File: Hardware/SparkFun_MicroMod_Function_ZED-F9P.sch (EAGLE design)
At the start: 121 parts, among them J2 MICROMOD_STANDARD, J3 QWIIC_RA, J4 U.FL, Q1 DMP21D0UT, U1 EEPROM, U2 U-BLOX_ZED-F9P, U3 FIN1017MXSOIC-8, U4 SN74AUP1T04DCK, U5 PCA9306DCUR, U6 74LVC541ABQ, U7 MIC5219 3.3V, U8 MIC5219 3.3V, U9 74LVC541ABQ

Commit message: Changed power resistor, needed higher power rating.
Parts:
- removed R22: 20, SparkFun-Resistors:20OHM-0603-1/10W-1%
- added R27: RK73H2ETTD16R9F, MicroMod_Function_GNSS_ublox_ZED_F9P:RK73H2ETTD16R9F
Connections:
- net ANT_!SHORT!: now also R27.1; no longer R22.1
- net N$49: now also R27.2; no longer R22.2
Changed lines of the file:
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@@
 <part name="R25" library="SparkFun-Resistors" deviceset="10KOHM" device="-0603-1/10W-1%" value="10k"/>
 <part name="L1" library="MicroMod_Function_GNSS_ublox_ZED_F9P" deviceset="LQW15AWR15J80D" device=""/>
-<part name="R22" library="SparkFun-Resistors" deviceset="20OHM" device="-0603-1/10W-1%" value="20"/>
 <part name="R23" library="SparkFun-Resistors" deviceset="2.0KOHM" device="-0603-1/10W-5%" value="2.0k"/>
 <part name="SUPPLY34" library="SparkFun-PowerSymbols" deviceset="VDD" device=""/>
@@
 <part name="TP19" library="SparkFun-Connectors" deviceset="TEST-POINT" device="3"/>
 <part name="TP20" library="SparkFun-Connectors" deviceset="TEST-POINT" device="3"/>
+<part name="R27" library="MicroMod_Function_GNSS_ublox_ZED_F9P" deviceset="RK73H2ETTD16R9F" device=""/>
 </parts>
 <sheets>
@@
 <attribute name="INDUCTANCE" x="228.6" y="223.52" size="2.032" layer="96" font="vector"/>
 </instance>
-<instance part="R22" gate="G$1" x="200.66" y="226.06" smashed="yes">
-<attribute name="NAME" x="200.66" y="227.584" size="1.778" layer="95" font="vector" align="bottom-center"/>
-<attribute name="VALUE" x="200.66" y="224.536" size="1.778" layer="96" font="vector" align="top-center"/>
-</instance>
 <instance part="R23" gate="G$1" x="190.5" y="203.2" smashed="yes" rot="R90">
 <attribute name="NAME" x="188.976" y="203.2" size="1.778" layer="95" font="vector" rot="R90" align="bottom-center"/>
@@
 <instance part="TP20" gate="G$1" x="152.4" y="236.22" smashed="yes" rot="R90">
 <attribute name="NAME" x="149.86" y="241.3" size="1.778" layer="95" font="vector"/>
+</instance>
+<instance part="R27" gate="G$1" x="200.66" y="226.06" smashed="yes">
+<attribute name="NAME" x="200.66" y="227.584" size="1.778" layer="95" font="vector" align="bottom-center"/>
+<attribute name="RESISTANCE" x="198.12" y="223.52" size="1.778" layer="96" font="vector"/>
 </instance>
 </instances>
@@
 <junction x="190.5" y="210.82"/>
 <label x="182.88" y="210.82" size="1.27" layer="95" rot="R180" xref="yes"/>
-<pinref part="R22" gate="G$1" pin="1"/>
 <pinref part="R23" gate="G$1" pin="2"/>
+<pinref part="R27" gate="G$1" pin="1"/>
 </segment>
 </net>
@@
 <junction x="220.98" y="226.06"/>
 <pinref part="L1" gate="G$1" pin="1"/>
-<pinref part="R22" gate="G$1" pin="2"/>
-</segment>
-</net>
+<pinref part="R27" gate="G$1" pin="2"/>
+</segment>
+</net>

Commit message: Ran ERC and updated.
Needed to re-place U3 parts. Needed to approve warnings/errors.
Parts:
- removed U$7: OPA344, SparkFun-IC-Amplifiers:OPA344
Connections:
- removed net GND2: JP10.2, JP2.2, JP3.2, JP4.1, JP5.1, JP6.1, JP8.2, JP9.2
- removed net N$13: C2.1, U1.VCC
- removed net N$18: J2.A0
- removed net N$31: J2.USB_VIN
- removed net N$33: J2.USBHOST_D-
- removed net N$34: J2.USBHOST_D+
- removed net N$35: J2.CTS
- removed net N$36: J2.RTS
- removed net N$37: J2.CAN-TX
- removed net N$38: J2.CAN-RX
- net 3.3V: now also C2.1, U1.VCC
- net ANT_DETECT: now also U$3G1.OUT; no longer U$7G1.OUT
- net GND: now also JP10.2, JP2.2, JP3.2, JP4.1, JP5.1, JP6.1, JP8.2, JP9.2
- net N$48: now also U$3G1.+IN; no longer U$7G1.+IN
- net N$49: now also U$3G1.-IN; no longer U$7G1.-IN
- net PWR_EN: now also U7.EN
- net VCC: no longer U7.EN

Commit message: Updated Schematic for ERC and comments from Paul.
Created NO jumper on USB-C shield/gnd tie.
Updated some power connections for style.
Deleted $ from designations.
Reworded ANT_OFF comment.
Repositioned ANT_!SHORT! net.
Floated U9Y7 output.
Renamed version back to v01 per SFE standards.
Changed proportional text to vector.
Ran and mitigated ERC.
Reworded LED comment.
Deleted unused wires.
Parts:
- added JP13: JUMPER-SMT_2_NO_SILK, SparkFun-Jumpers:JUMPER-SMT_2_NO_SILK
- added R22: 10k, SparkFun-Resistors:10KOHM-0603-1/10W-1%
- renumbered U$3 to U10
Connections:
- removed net N$49: C13.1, L1.1, R27.2, U10G1.-IN
- new net N$18: J1.SHLD, JP13.2
- net ANT_!SHORT!: now also C13.1, L1.1, R27.2, U10G1.-IN
- net GND: now also JP13.1; no longer J1.SHLD, U9.Y7
- net PWR_EN: now also R22.1
- net VCC: now also R22.2
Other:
- note added: "Cut jumpers to disable LEDs."
- note added: "Move R25 to R26 to use antenna supervisor."
- note added: "v01"
- note removed: "Cut jumpers to remove respective LEDs"
- note removed: "Pull ANT_OFF High to use antenna supervisor."
- note removed: "v1.0"

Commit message: Update Post schematic review.
Made all easy changes, in midst of redoing decoupling per requests.
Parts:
- removed BYP, JP7, USB_EN: JUMPER-SMT_2_NO_SILK, SparkFun-Jumpers:JUMPER-SMT_2_NO_SILK
- removed C3, C5: 470pF, SparkFun-Capacitors:470PF-0603-50V-5%
- removed C4, C6: 2.2uF, SparkFun-Capacitors:2.2UF-0603-10V-20%
- removed D1, D12, D2, D8: RED, SparkFun-LED:LED-RED0603
- removed D10: 3A/10V/280mV, SparkFun-DiscreteSemi:DIODE-SCHOTTKY-BAT60A
- removed F1: 6V/2A, SparkFun-Fuses:PPTC_6V2A
- removed JP10, JP2, JP3, JP8: JUMPER-SMT_2_NC_TRACE_SILK, SparkFun-Jumpers:JUMPER-SMT_2_NC_TRACE_SILK
- removed JP11, JP12: JUMPER-SMT_3_2-NC_TRACE_SILK, SparkFun-Jumpers:JUMPER-SMT_3_2-NC_TRACE_SILK
- removed R13, R14, R15, R16: 1.5k, SparkFun-Resistors:1.5KOHM-0603-1/10W-1%
- removed R17: 100k, SparkFun-Resistors:100KOHM-0603-1/10W-1%
- removed R19, R21, R4: 1k, SparkFun-Resistors:1KOHM-0603-1/10W-1%
- removed R22: 10k, SparkFun-Resistors:10KOHM-0603-1/10W-1%
- removed U7, U8: MIC5219 3.3V, SparkFun-IC-Power:V_REG_MIC52193.3V
- added C18: 2.2uF, SparkFun-Capacitors:2.2UF-0402_TIGHT-10V-10%-X5R
- added C19, C20: 0.1uF, SparkFun-Capacitors:0.1UF-0603-25V-(+80/-20%)
- added J8: Bus Selection, SparkFun-Connectors:CONN_03LOCK
- added J9: (no value), SparkFun-Connectors:CONN_02
- added U$21, U$22: 74LVC4066D_QUAD_BILATERAL_SWITCH, SparkFun-IC-Logic:74LVC4066D_QUAD_BILATERAL_SWITCH
- C11: device SparkFun-Capacitors:0.1UF-0402-16V-10% -> SparkFun-Capacitors:0.1UF-0603-25V-(+80/-20%)
- J4: device SparkFun-RF:ANTENNA-SMA-GROUNDEDEDGE_SMA -> SparkFun-Connectors:U.FL2PIN
- J5: value (none) -> 455-1750-1-ND; device SparkFun-Connectors:CONN_02-JST-2MM-SMT -> SparkFun-Connectors:CONN_03
- J6: device SparkFun-Connectors:CONN_01 -> SparkFun-Connectors:CONN_04PTH
- R10, R9: value 27OHM -> 27
- R27: value RK73H2ETTD16R9F -> 10; device MicroMod_Function_GNSS_ublox_ZED_F9P:RK73H2ETTD16R9F -> SparkFun-Resistors:10OHM-0603-1/10W-1%
- R3: value 1k -> 10k; device SparkFun-Resistors:1KOHM-0603-1/10W-1% -> SparkFun-Resistors:10KOHM-0603-1/10W-1%
- U9: value 74LVC541ABQ -> SN74AUP1T04DCK; device MicroMod_Function_GNSS_ublox_ZED_F9P:74LVC541ABQ -> MicroMod_Function_GNSS_ublox_ZED_F9P:SN74AUP1T04DCK
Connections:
- removed net N$11: D1.C, R3.2
- removed net N$14: C5.1, U8.BP
- removed net N$15: JP8.1, R19.1
- removed net N$16: D8.C, R19.2
- removed net N$17: C3.1, U7.BP
- removed net N$19: D10.A, USB_EN.2
- removed net N$20: BYP.1, D10.C, D9.C, F1.1
- removed net N$24: JP7.2, R17.1, U6.A7
- removed net N$39: JP10.1, R21.1
- removed net N$40: D12.C, R21.2
- removed net N$42: JP12.1, R14.2
- removed net N$43: JP11.1, R15.2
- removed net N$44: JP11.3, R16.2
- removed net N$47: JP12.3, R13.2
- removed net N$50: J5.2, U3.DO+
- removed net N$7 (its old number): D2.C, R4.2
- new net !ZED_DSEL!: U$22.1E, U$22.2E, U$22.3E, U$22.4E, U9.Y
- new net N$13: Q1.D, R23.2, R27.1
- new net PICO: U$22.4Z
- new net POCI: U$22.3Z
- new net RXI: U$21.4Z
- new net SCK: U$22.2Z
- new net SCL: U$21.2Z
- new net SDA: U$21.1Z
- new net SPI_!CS!: U$22.1Z
- new net TXO: U$21.3Z
- net !SAFEBOOT!: now also J7.1; no longer J2.F5, U6.A3
- net 3.3V: no longer D2.A, JP11.2
- net ANT_!SHORT!: no longer Q1.D, R23.2, R27.1, U6.A6
- net ANT_DETECT: no longer U6.A5
- net ANT_OFF: no longer U9.Y0
- net EXTINT: now also J9.1, U6.A3; no longer U6.A4
- net GEO_STAT: now also U6.Y6; no longer U9.Y1
- net GND: now also C11.1, C19.2, C20.2, J5.3, J6.1, J6.4, J8.3, J9.2, U$21.GND, U$22.GND; no longer C11.2, C3.2, C5.2, JP10.2, JP2.2, JP3.2, JP7.1, JP8.2, U7.GND, U8.GND, U9.A7
- net GND_RF: now also C18.2; no longer C4.2, C6.2
- net IO_!OE!: no longer U9.!OE1!, U9.!OE2!
- net N$10: now also J8.1; no longer JP2.1
- net N$51: now also J6.3; no longer J5.1
- net N$9: now also J6.2, U3.DO+; no longer JP3.1, R4.1
- net PPS: now also U6.Y5; no longer U9.Y6
- net PWR_EN: no longer R22.1, U7.EN
- net RTK_STAT: now also U6.Y7; no longer U9.Y2
- net RX/COPI: no longer U6.A1
- net RX2/RTCM: now also J5.1; no longer J2.F7, J6.1
- net SCL/SCK: no longer R16.1
- net SDA/!CS!: no longer R15.1
- net TX/CIPO: no longer U9.Y4
- net TX2/RTCM: now also J5.2, U6.Y1; no longer J2.F6, J7.1, U9.Y3
- net TX_READY: now also U6.Y4; no longer U9.Y5
- net VCC: now also D9.C; no longer BYP.2, F1.2, R22.2, U7.IN
- net VDD: now also C11.2, C19.1, C20.1, R3.2, U$21.VCC, U$22.VCC; no longer C11.1, C4.1, JP12.2, R17.2, U7.OUT, U8.EN
- net VIN: no longer D1.A
- net V_BATT: now also C18.1
- net V_USB: no longer D8.A, U8.IN, USB_EN.1
- net V_USB_2: no longer C6.1, D12.A, U8.OUT
- net ZED_!SAFEBOOT!: no longer U6.Y3
- net ZED_ANT_!SHORT!: no longer U6.Y6
- net ZED_ANT_DETECT: no longer U6.Y5
- net ZED_ANT_OFF: no longer U9.A0
- net ZED_DSEL: now also J8.2, U$21.1E, U$21.2E, U$21.3E, U$21.4E, U9.A; no longer U6.Y7
- net ZED_EXTINT: now also U6.Y3; no longer U6.Y4
- net ZED_GEO_STAT: now also U6.A6; no longer U9.A1
- net ZED_PPS: now also U6.A5; no longer U9.A6
- net ZED_RTK_STAT: now also U6.A7; no longer U9.A2
- net ZED_RX/COPI: no longer U6.Y1
- net ZED_SCL/SCK: no longer R14.1
- net ZED_SDA/!CS!: no longer R13.1
- net ZED_TX/CIPO: no longer U9.A4
- net ZED_TX2/RTCM: now also U6.A1; no longer U9.A3
- net ZED_TX_READY: now also U6.A4; no longer U9.A5
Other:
- note added: "Bus Selection: 74LVC4066D"
- note added: "Differential PPS"
- note added: "GNSS Module ZED-F9P"
- note added: "RF/Antenna Supervision"
- note added: "SPI or I2C+Serial Selection"
- note added: "The default is I2C and Serial."
- note added: "To use SPI simply move the 2-pin jumper to the side labeled "SPI"."
- note removed: "Close to enable SPI."
- note removed: "Close to enable USB power-up."
- note removed: "GPS Module ZED-F9P"
- note removed: "NO"
- note removed: "RF/ANTENNA SUPERVISION"
- note removed: "Tantalum"
- moved on the sheet: C1, C10, C11, C12, C13, C14, C15, C16, C17, C2, C7, C8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

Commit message: Complete schematic after DR changes.
Reorganized power: changed supply, removed fuse, replaced usb_det supply with voltage divider, renamed power nets.
Added TPs and PTH breakouts for some pins.
Changed I/O decoupling: Replaced octal buffer with 2x quad SSR switches, removed buffer on antenna supervision, rearranged pins on remaining octal buffer.
Labeled diff PPS signal.
Added second Qwiic connector.
Added selector headers for bus and antenna supervisor circuits.
Removed extra LEDs.
Replaced SMA with u.FL.
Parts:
- removed C16: 0.1uF, SparkFun-Capacitors:0.1UF-0603-25V-(+80/-20%)
- removed D5: BLUE, SparkFun-LED:LED-BLUE0603
- removed JP6: JUMPER-SMT_2_NC_TRACE_SILK, SparkFun-Jumpers:JUMPER-SMT_2_NC_TRACE_SILK
- removed R25: 10k, SparkFun-Resistors:10KOHM-0603-1/10W-1%
- removed R26: DNP, SparkFun-Resistors:DNP-0603_NO_CREAM
- removed TP11: TEST-POINT3, SparkFun-Connectors:TEST-POINT3
- removed U$21, U$22: 74LVC4066D_QUAD_BILATERAL_SWITCH, SparkFun-IC-Logic:74LVC4066D_QUAD_BILATERAL_SWITCH
- added C3: 1.0uF, SparkFun-Capacitors:1.0UF-0603-16V-10%
- added D1: 3A/10V/280mV, SparkFun-DiscreteSemi:DIODE-SCHOTTKY-BAT60A
- added J10: QWIIC_RA, SparkFun-Connectors:QWIIC_CONNECTORJS-1MM
- added J11: Bus Selection, SparkFun-Connectors:CONN_03LOCK
- added J12: USB Female Type C Connector, SparkFun-Connectors:USB_C_4-LAYER-ISOLATED
- added J13, J14, J15, J16, J17: (no value), SparkFun-Connectors:CONN_01
- added J18: (no value), SparkFun-Connectors:CONN_02
- added JP2: JUMPER-SMT_2_NO_SILK, SparkFun-Jumpers:JUMPER-SMT_2_NO_SILK
- added R4: 10k, SparkFun-Resistors:10KOHM-0603-1/10W-1%
- added U11, U12: 74LVC4066D_QUAD_BILATERAL_SWITCH, SparkFun-IC-Logic:74LVC4066D_QUAD_BILATERAL_SWITCH
- added U7: 3.3V, SparkFun-IC-Power:V_REG_AP2112K-3.3V
- C1: value 10pF -> 1.0uF; device SparkFun-Capacitors:10PF-0603-50V-5% -> SparkFun-Capacitors:1.0UF-0603-16V-10%
- J1: device SparkFun-Connectors:USB_C_2-LAYER_PADS -> SparkFun-Connectors:CONN_01
- R12: value 220k -> 68.1k; device SparkFun-Resistors:220KOHM-0603-1/10W-1% -> SparkFun-Resistors:68.1KOHM-0603-1/10W-1%
- R7: value 1k -> 10k; device SparkFun-Resistors:1KOHM-0603-1/10W-1% -> SparkFun-Resistors:10KOHM-0603-1/10W-1%
- TP7, TP9: value TEST-POINTPOGO_PTH -> TEST-POINT3; device SparkFun-Connectors:TEST-POINTPOGO_PTH -> SparkFun-Connectors:TEST-POINT3
- U5: value PCA9306DCUR -> SN74LVC1G66DRYR; device MicroMod_Function_GNSS_ublox_ZED_F9P:PCA9306DCUR -> MicroMod_Function_GNSS_ublox_ZED_F9P:SN74LVC1G66DRYR
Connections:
- removed net N$18: J1.SHLD, JP13.2
- removed net N$45: JP6.2, R7.1
- removed net N$46: D5.C, R7.2
- removed net PICO: U$22.4Z
- removed net POCI: U$22.3Z
- removed net RX/COPI: J2.RX, J2.SPI_SDI, TP15.1
- removed net RXI: U$21.4Z
- removed net SCK: U$22.2Z
- removed net SCL: U$21.2Z
- removed net SCL/SCK: J2.I2C_SCL, J2.SPI_SCK, J3.4, TP19.1, U1.SCL, U5.SCL1
- removed net SDA: U$21.1Z
- removed net SDA/!CS!: J2.F1/!CS!, J2.I2C_SDA, J3.3, TP20.1, U1.SDA, U5.SDA1
- removed net SPI_!CS!: U$22.1Z
- removed net TX/CIPO: J2.SPI_SDO, J2.TX, TP16.1
- removed net TXO: U$21.3Z
- removed net VCC: C12.1, D9.C, TP6.1, U3.VCC
- removed net V_USB_2: C7.1, C8.1, R18.2, TP11.1, U2.V_USB
- new net 5V: C3.1, D1.C, D9.C, U5.CTRL_IN, U5.VCC, U7.IN
- new net MM_!CS!: J2.F1/!CS!, TP8.1, U12.1Z
- new net MM_CIPO: J2.SPI_SDO, TP6.1, U12.3Z
- new net MM_COPI: J2.SPI_SDI, TP2.1, U12.4Z
- new net MM_RX: J2.RX, TP15.1, U11.4Z
- new net MM_SCK: J2.SPI_SCK, TP7.1, U12.2Z
- new net MM_SCL: J10.4, J2.I2C_SCL, J3.4, TP19.1, U1.SCL, U11.2Z
- new net MM_SDA: J10.3, J2.I2C_SDA, J3.3, TP20.1, U1.SDA, U11.1Z
- new net MM_TX: J2.TX, TP16.1, U11.3Z
- new net N$11: J11.1, R4.1
- new net N$16: D1.A, JP2.2
- new net SHLD: J12.SHLD, JP13.1
- new net V_ZED: C10.1, C11.2, C14.2, C17.2, C19.1, C20.1, C9.1, D11.A, U10G2.P$V+, U11.VCC, U12.VCC, U2.VCC, U4.A, U4.VCC, U6.VCC, U9.VCC
- new net ZED_USB_DET: C7.1, C8.1, R12.1, R12.2, R18.2, U2.V_USB, U5.A_OUT
- net !RESET!: now also J18.1, U6.A1; no longer U6.A2
- net !ZED_DSEL!: now also U12.1E, U12.2E, U12.3E, U12.4E; no longer U$22.1E, U$22.2E, U$22.3E, U$22.4E
- net 3.3V: now also C12.1, J10.2, U3.VCC; no longer C16.1, TP8.1, U5.VREF1
- net ANT_OFF: now also J11.2; no longer R25.2, R26.1
- net EXTINT: now also TP10.1, U6.A2; no longer U6.A3
- net GEO_STAT: now also J2.F5, U6.Y7; no longer D5.A, U6.Y6
- net GND: now also C3.2, J10.1, J12.GND, J13.1, J14.1, J18.2, JP13.2, U5.VSS, U7.GND; no longer C10.2, C11.1, C16.2, C17.1, C19.2, C20.2, J1.GND, J8.3, JP13.1, JP6.1, TP2.1, TP7.1, U$21.GND, U$22.GND, U4.GND, U5.GND, U6.GND, U9.GND
- net GND_RF: now also C10.2, C11.1, C17.1, C19.2, C20.2, J15.1, J16.1, J8.3, R7.1, U11.GND, U12.GND, U4.GND, U6.GND, U9.GND; no longer R25.1, TP9.1
- net N$1: now also J12.D+; no longer J1.D+
- net N$12: now also J11.3, R7.2; no longer C1.1, R12.1, U5.EN, U5.VREF2
- net N$2: now also J12.D-; no longer J1.D-
- net N$3: now also J12.CC2; no longer J1.CC2
- net N$4: now also J12.CC1; no longer J1.CC1
- net PPS: now also U6.Y0; no longer U6.Y5
- net PWR_EN: now also U7.EN
- net RTK_STAT: now also J2.F6, U6.Y6; no longer U6.Y7
- net RX2/RTCM: now also U6.A5; no longer U6.A0
- net TX2/RTCM: now also U6.Y4; no longer U6.Y1
- net TX_READY: now also TP9.1, U6.Y3; no longer U6.Y4
- net VDD: now also C1.1, J1.1, U7.OUT; no longer C10.1, C11.2, C14.2, C17.2, C19.1, C20.1, C9.1, D11.A, R12.2, U$21.VCC, U$22.VCC, U10G2.P$V+, U2.VCC, U4.A, U4.VCC, U6.VCC, U9.VCC
- net V_BATT: now also J17.1
- net V_RF: now also R4.2; no longer R26.2
- net V_USB: now also J12.VBUS, JP2.1, U5.A_IN; no longer J1.VBUS, TP10.1
- net ZED_!RESET!: now also U6.Y1; no longer U6.Y2
- net ZED_DSEL: now also U11.1E, U11.2E, U11.3E, U11.4E; no longer U$21.1E, U$21.2E, U$21.3E, U$21.4E
- net ZED_EXTINT: now also U6.Y2; no longer U6.Y3
- net ZED_GEO_STAT: now also U6.A7; no longer U6.A6
- net ZED_PPS: now also U6.A0; no longer U6.A5
- net ZED_RTK_STAT: now also U6.A6; no longer U6.A7
- net ZED_RX/COPI: now also U11.4Y, U12.4Y
- net ZED_RX2/RTCM: now also U6.Y5; no longer U6.Y0
- net ZED_SCL/SCK: now also U11.2Y, U12.2Y; no longer U5.SCL2
- net ZED_SDA/!CS!: now also U11.1Y, U12.1Y; no longer U5.SDA2
- net ZED_TX/CIPO: now also U11.3Y, U12.3Y
- net ZED_TX2/RTCM: now also U6.A4; no longer U6.A1
- net ZED_TX_READY: now also U6.A3; no longer U6.A4
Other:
- note added: "Close to enable USB power."
- note added: "I/O Control"
- note added: "Move jumper to 1-2 to enable antenna supervisor."
- note added: "Power Supply"
- note added: "SPI || I2C+Serial Selection"
- note added: "Test Points and Breakouts"
- note removed: "Cut jumpers to remove I2C pullups from bus"
- note removed: "External Breakout"
- note removed: "I/O Decoupling Control"
- note removed: "I2C Decoupling"
- note removed: "Move R25 to R26 to use antenna supervisor."
- note removed: "Power Supplies"
- note removed: "SPI or I2C+Serial Selection"
- moved on the sheet: BT1, C1, C10, C11, C12, C13, C14, C15, C17, C18, C19, C2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

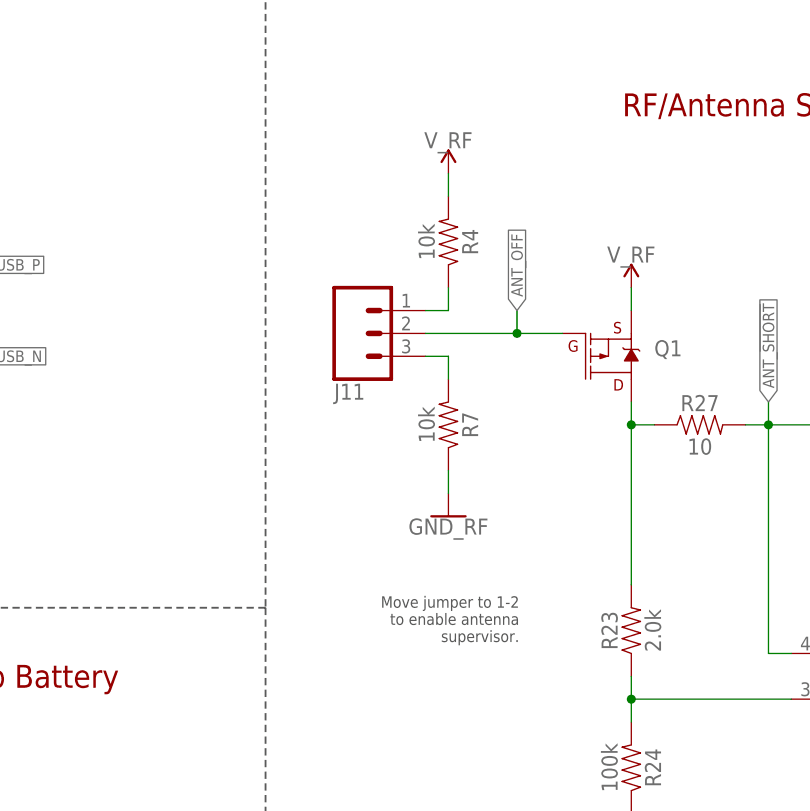
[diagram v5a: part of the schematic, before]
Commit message: Update selector wording per PC.
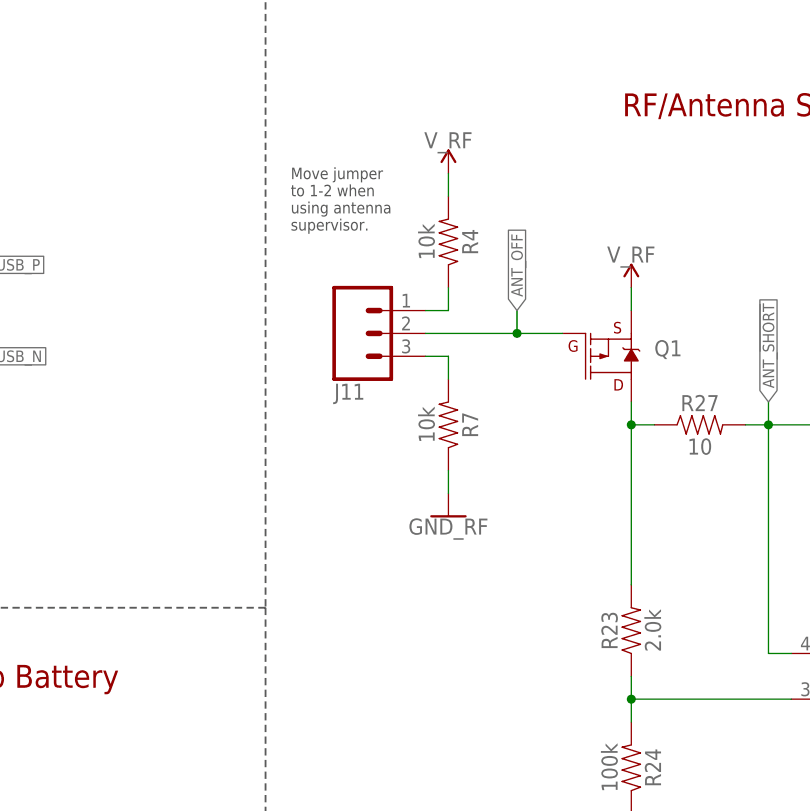
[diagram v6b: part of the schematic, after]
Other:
- note added: "Move jumper to 1-2 when using antenna supervisor."
- note removed: "Move jumper to 1-2 to enable antenna supervisor."
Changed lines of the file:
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@@
 close to
 connector.</text>
-<text x="175.514" y="207.01" size="1.27" layer="97" font="vector" align="bottom-right">Move jumper to 1-2
-to enable antenna
+<text x="150.114" y="252.73" size="1.27" layer="97" font="vector">Move jumper
+to 1-2 when
+using antenna
 supervisor.</text>
 <wire x1="350.52" y1="66.04" x2="431.8" y2="66.04" width="0.2032" layer="97" style="longdash"/>
